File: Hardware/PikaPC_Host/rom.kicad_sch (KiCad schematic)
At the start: 2 parts, among them U5 SST39VF010

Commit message: Annotate & prep for output - Host & KBC
add gerber output to gitignore
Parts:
- C35: Mouser (none) -> 187-CL21B104KACNNNC
- U5: Mouser (none) -> 804-39VF0107INHE-T
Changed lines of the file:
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@@
+			)
+		)
+		(property "Mouser" "804-39VF0107INHE-T "
+			(at 139.7 93.98 0)
+			(effects
+				(font
+					(size 1.27 1.27)
+				)
+				(hide yes)
 			)
 		)
@@
 			(effects
 				(font
+					(size 1.27 1.27)
+				)
+				(hide yes)
+			)
+		)
+		(property "Mouser" "187-CL21B104KACNNNC"
+			(at 154.94 92.71 90)
+			(effects
+				(font

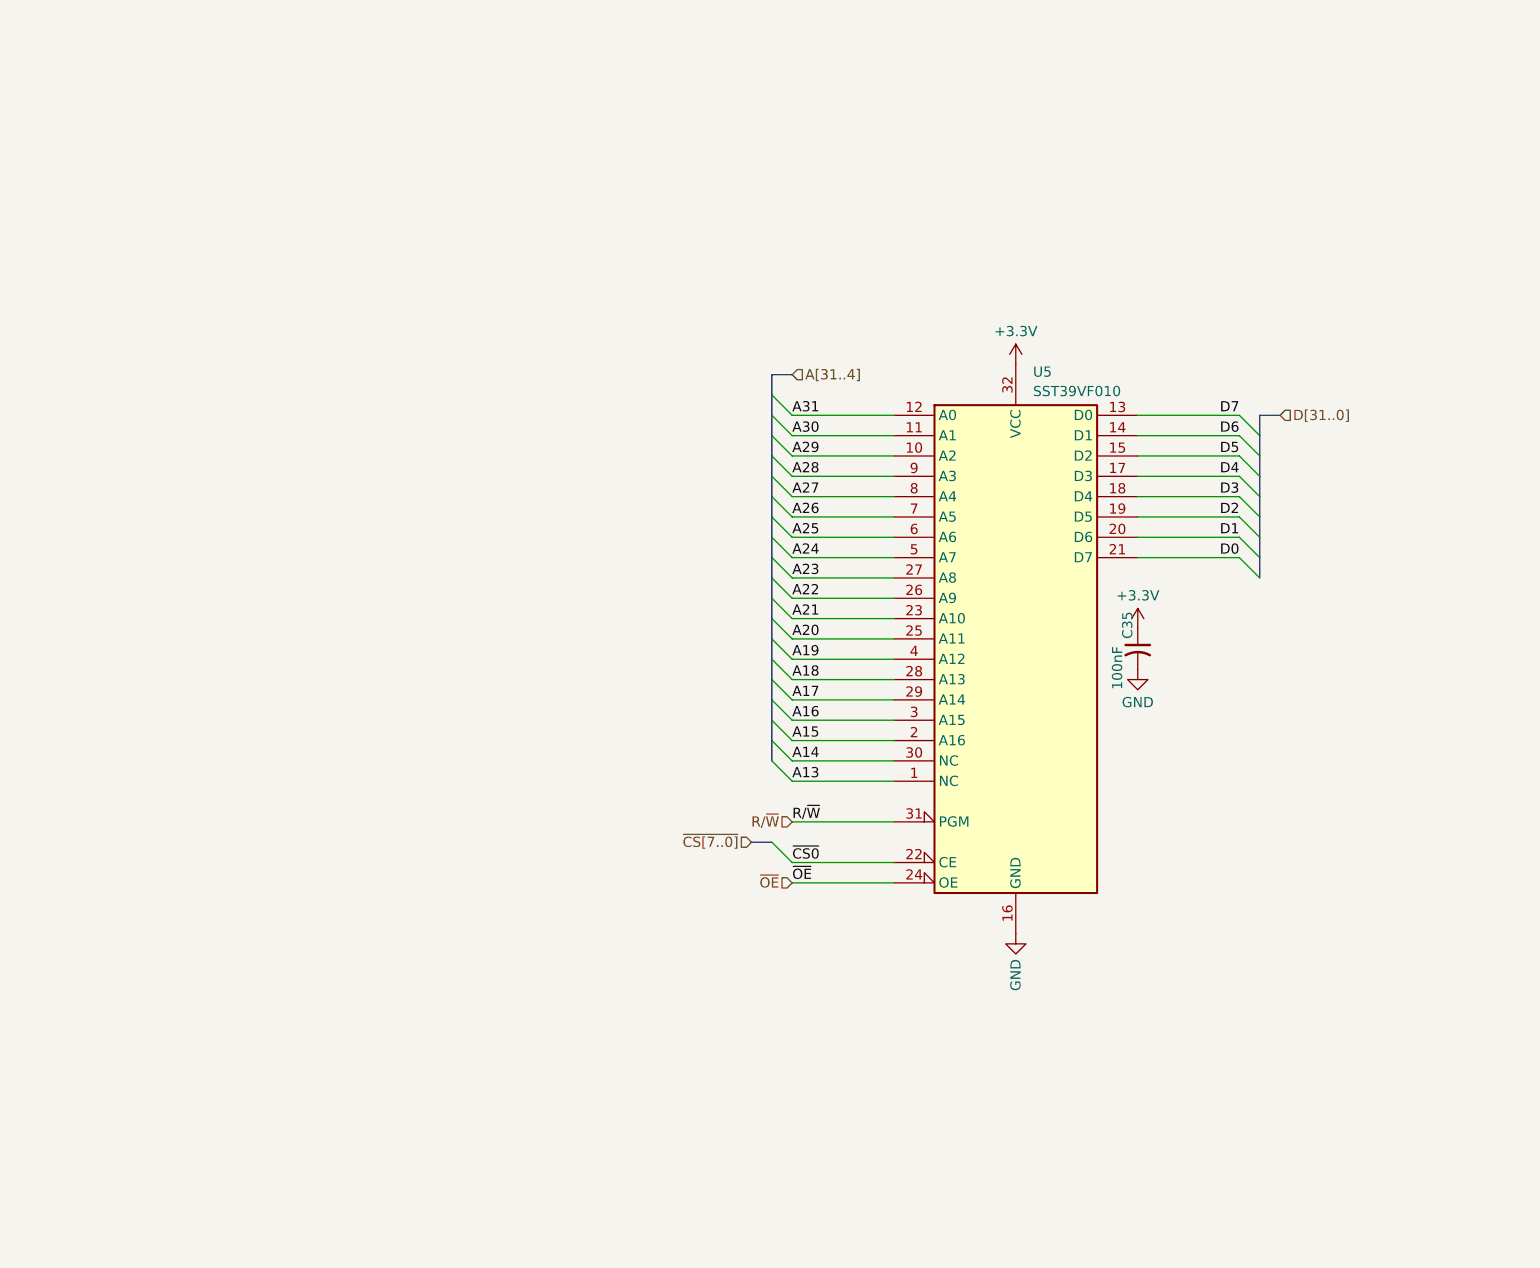
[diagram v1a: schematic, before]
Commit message: Host Card updates
- add missing bus pull-ups
- add on-board DRAM
- add series termination resistors to AD bus
- fix DE9 footprint mounting hole location
- fix double-buffered bus clock
- use 74'2244 buffer w/series term resistors for bus control signals
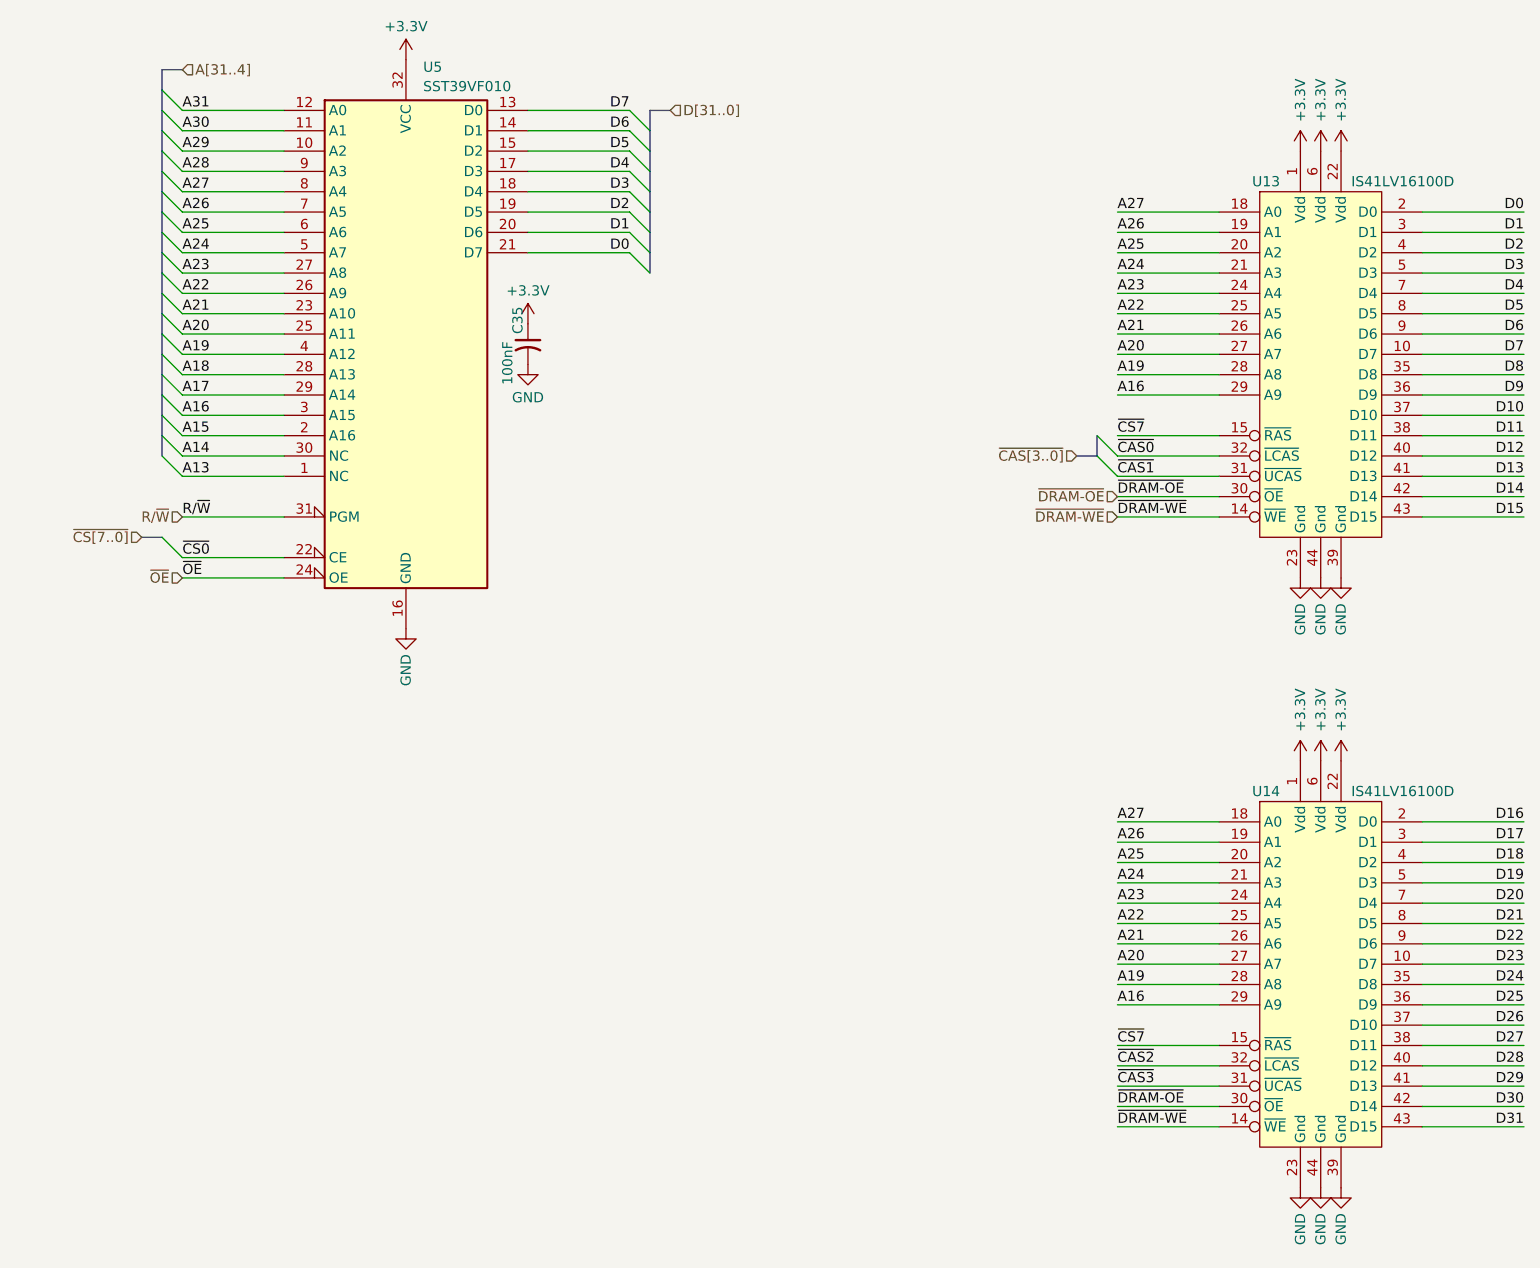
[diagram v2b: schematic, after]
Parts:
- added U13, U14: IS41LV16100D, PikaPC_Host:TSOP-II-44, symbol PikaPC:IS41LV16100D
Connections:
- net +3.3V: now also U13.1 (Vdd), U13.22 (Vdd), U13.6 (Vdd), U14.1 (Vdd), U14.22 (Vdd), U14.6 (Vdd)
- net A16: now also U13.29 (A9), U14.29 (A9)
- net A19: now also U13.28 (A8), U14.28 (A8)
- net A20: now also U13.27 (A7), U14.27 (A7)
- net A21: now also U13.26 (A6), U14.26 (A6)
- net A22: now also U13.25 (A5), U14.25 (A5)
- net A23: now also U13.24 (A4), U14.24 (A4)
- net A24: now also U13.21 (A3), U14.21 (A3)
- net A25: now also U13.20 (A2), U14.20 (A2)
- net A26: now also U13.19 (A1), U14.19 (A1)
- net A27: now also U13.18 (A0), U14.18 (A0)
- net D0: now also U13.2 (D0)
- net D1: now also U13.3 (D1)
- net D2: now also U13.4 (D2)
- net D3: now also U13.5 (D3)
- net D4: now also U13.7 (D4)
- net D5: now also U13.8 (D5)
- net D6: now also U13.9 (D6)
- net D7: now also U13.10 (D7)
- net GND: now also U13.23 (Gnd), U13.39 (Gnd), U13.44 (Gnd), U14.23 (Gnd), U14.39 (Gnd), U14.44 (Gnd)
- new net: U13.11 (NC), U13.12 (NC), U13.13 (NC), U13.16 (NC), U13.17 (NC), U13.33 (NC), U13.34 (NC)
- new net: U14.11 (NC), U14.12 (NC), U14.13 (NC), U14.16 (NC), U14.17 (NC), U14.33 (NC), U14.34 (NC)
- new net D10: U13.37 (D10)
- new net D11: U13.38 (D11)
- new net D12: U13.40 (D12)
- new net D13: U13.41 (D13)
- new net D14: U13.42 (D14)
- new net D15: U13.43 (D15)
- new net D16: U14.2 (D0)
- new net D17: U14.3 (D1)
- new net D18: U14.4 (D2)
- new net D19: U14.5 (D3)
- new net D20: U14.7 (D4)
- new net D21: U14.8 (D5)
- new net D22: U14.9 (D6)
- new net D23: U14.10 (D7)
- new net D24: U14.35 (D8)
- new net D25: U14.36 (D9)
- new net D26: U14.37 (D10)
- new net D27: U14.38 (D11)
- new net D28: U14.40 (D12)
- new net D29: U14.41 (D13)
- new net D30: U14.42 (D14)
- new net D31: U14.43 (D15)
- new net D8: U13.35 (D8)
- new net D9: U13.36 (D9)
- new net ~{CAS0}: U13.32 (~{LCAS})
- new net ~{CAS1}: U13.31 (~{UCAS})
- new net ~{CAS2}: U14.32 (~{LCAS})
- new net ~{CAS3}: U14.31 (~{UCAS})
- new net ~{CS7}: U13.15 (~{RAS}), U14.15 (~{RAS})
- new net ~{DRAM-OE}: U13.30 (~{OE}), U14.30 (~{OE})
- new net ~{DRAM-WE}: U13.14 (~{WE}), U14.14 (~{WE})
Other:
- moved on the sheet: C35, U5
